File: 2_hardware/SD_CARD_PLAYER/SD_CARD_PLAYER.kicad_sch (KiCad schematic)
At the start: 125 parts, among them J1 Conn_02x05_Odd_Even, J10 SD_CARD_CONN, J11 Analogue Input Jack, J12 Analogue Input Jack, J2 audio output, J3 Digital Input Jack, J4 Digital Input Jack, J5 Digital Input Jack, J7 Digital Input Jack, Q1 MMBT3904, Q2 MMBT3904, Q3 MMBT3904, Q4 MMBT3904, SW1 SW_Push, SW2 SW_Push, SW3 SW_Push, SW4 SW_Push, SW5 SW_SPDT, U1 TL431DBZ, U2 PICO_RP2040, U3 74HC595, U4 MCP6232, U5 LM1117MP-5.0, U6 MCP6002-xMS

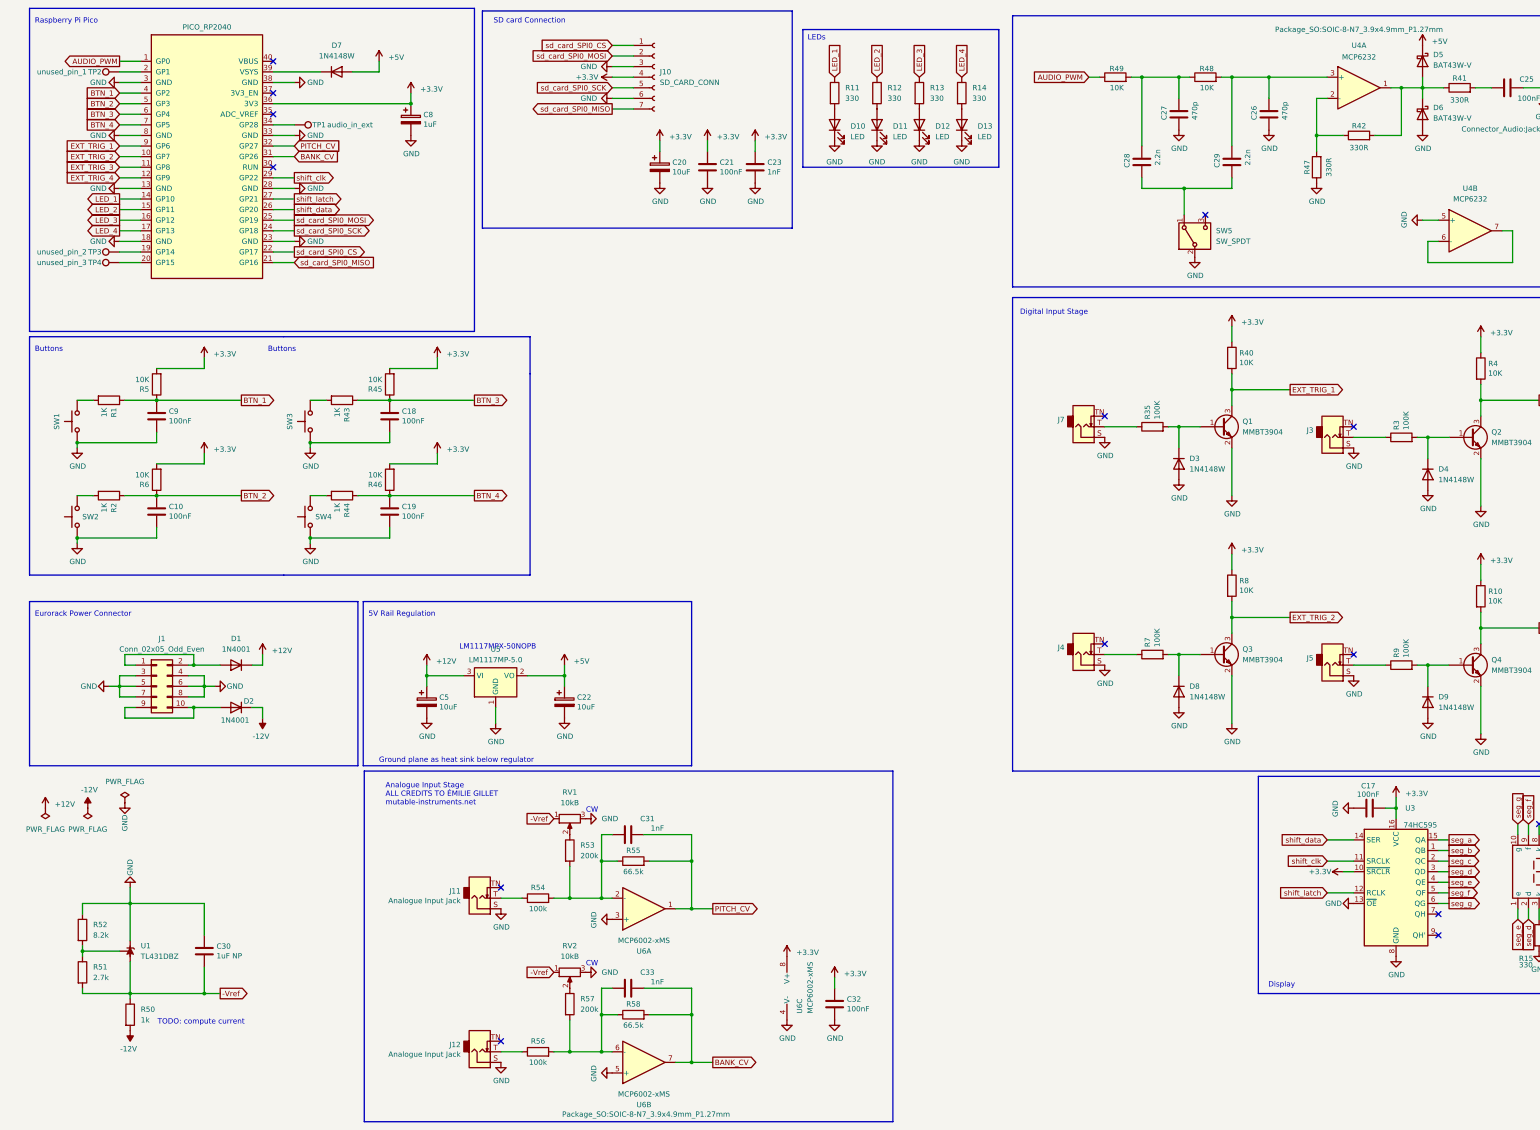
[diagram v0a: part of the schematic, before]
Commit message: Corrected -vref supply schematic, assigned correct footprint to lm4040B10
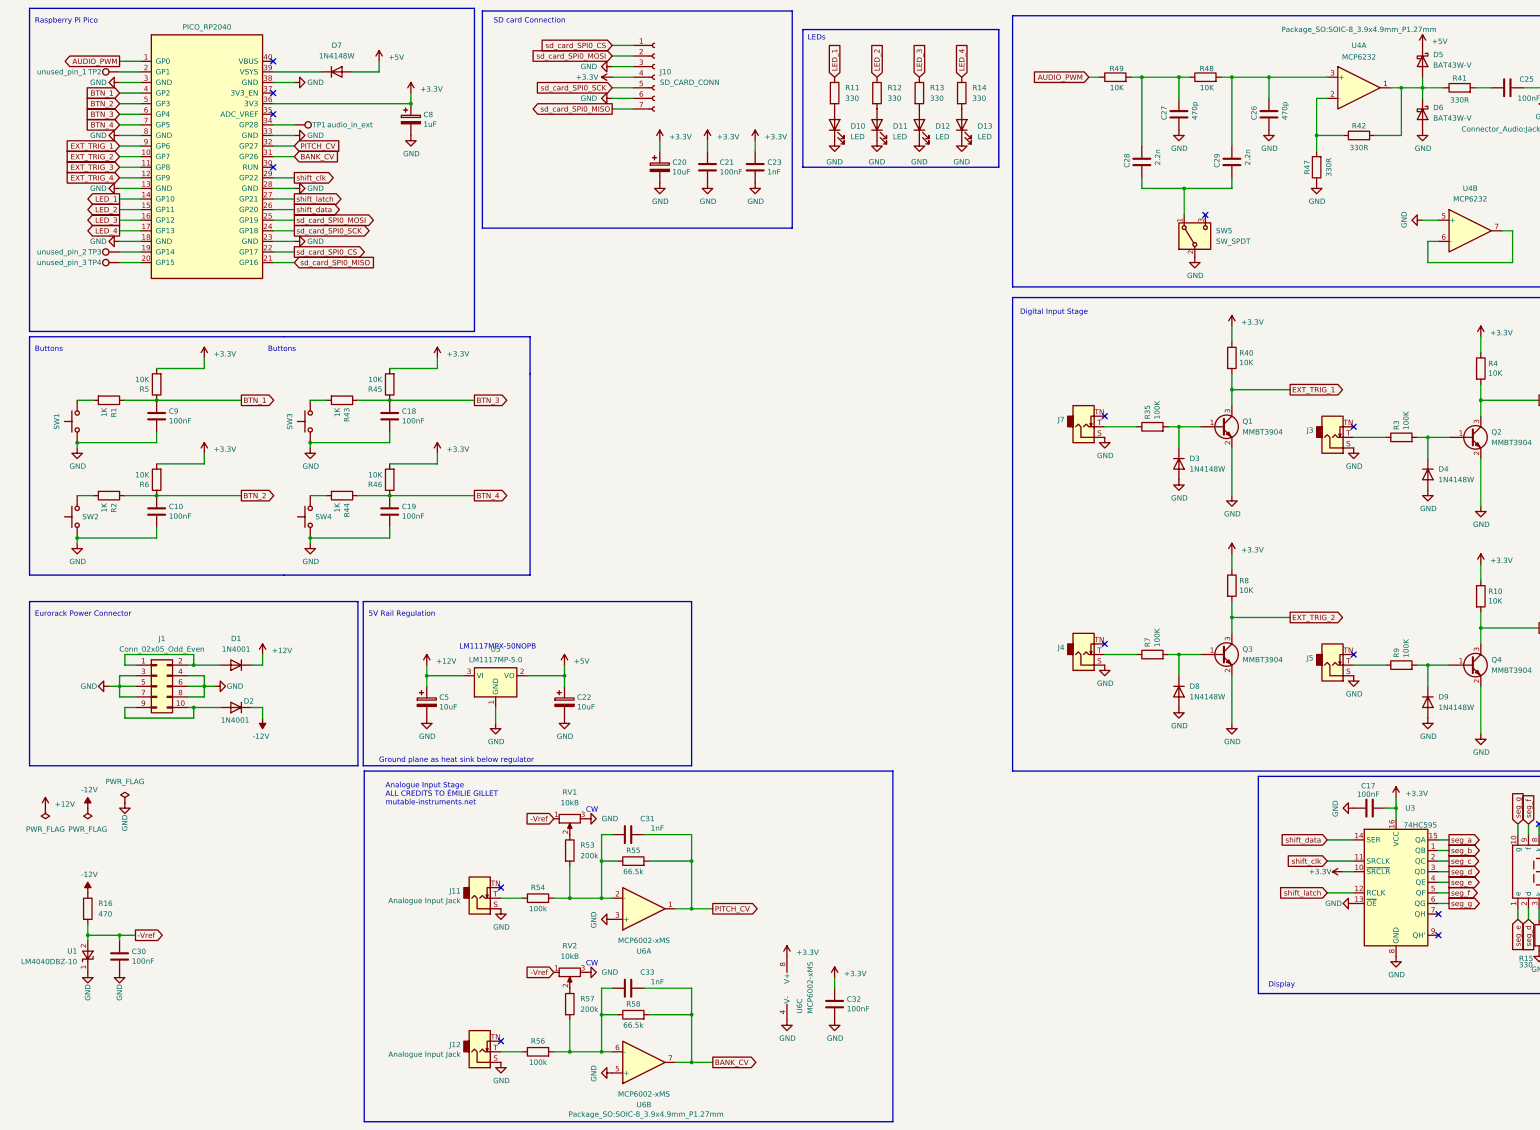
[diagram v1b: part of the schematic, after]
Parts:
- removed R50: 1k, Resistor_SMD:R_0805_2012Metric_Pad1.20x1.40mm_HandSolder, symbol Device:R
- removed R51: 2.7k, Resistor_SMD:R_0805_2012Metric_Pad1.20x1.40mm_HandSolder, symbol Device:R
- removed R52: 8.2k, Resistor_SMD:R_0805_2012Metric_Pad1.20x1.40mm_HandSolder, symbol Device:R
- removed U1: TL431DBZ, Package_TO_SOT_SMD:SOT-23, symbol Reference_Voltage:TL431DBZ
- added R16: 470, symbol Device:R
- added U1: LM4040DBZ-10, Package_TO_SOT_SMD:SOT-23, symbol Reference_Voltage:LM4040DBZ-10
- C30: value 1uF NP -> 100nF
- U4, U6: footprint Package_SO:SOIC-8-N7_3.9x4.9mm_P1.27mm -> Package_SO:SOIC-8_3.9x4.9mm_P1.27mm
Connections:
- net -12V: now also R16.1
- net -Vref: now also C30.1, R16.2, U1.2 (A); no longer C30.2
- net GND: now also C30.2, U1.1 (K); no longer C30.1
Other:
- note removed: "TODO: compute current"
- moved on the sheet: C30
